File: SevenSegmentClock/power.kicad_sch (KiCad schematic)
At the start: 0 parts

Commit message: Adding two more displays to show a degree and a percent symbols
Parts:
- added C?: 1uF, symbol Device:C_Polarized
- added C?: 470uF, symbol Device:C_Polarized
- added C?: 100nF, symbol Device:C
- added U?: LM2596S-3.3, Package_TO_SOT_SMD:TO-263-5_TabPin3, symbol Regulator_Switching:LM2596S-3.3
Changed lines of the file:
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@@
 (kicad_sch (version 20211123) (generator eeschema)
   (paper "A4")
+  (symbol (lib_id "Device:C_Polarized") (at 144.78 106.807 0) (unit 1)
+    (in_bom yes) (on_board yes) (fields_autoplaced)
+    (property "Reference" "C?" (id 0) (at 147.701 105.0833 0)
+      (effects (font (size 1.27 1.27)) (justify left))
+    )
+    (property "Value" "1uF" (id 1) (at 147.701 107.6202 0)
+      (effects (font (size 1.27 1.27)) (justify left))
+    )
+    (property "Footprint" "" (id 2) (at 145.7452 110.617 0)
+      (effects (font (size 1.27 1.27)) hide)
+    )
+    (property "Datasheet" "~" (id 3) (at 144.78 106.807 0)
+      (effects (font (size 1.27 1.27)) hide)
+    )
+    (pin "1")
+    (pin "2")
+  )
+  (symbol (lib_id "Regulator_Switching:LM2596S-3.3") (at 153.924 74.295 0) (unit 1)
+    (in_bom yes) (on_board yes) (fields_autoplaced)
+    (property "Reference" "U?" (id 0) (at 153.924 65.5152 0))
+    (property "Value" "LM2596S-3.3" (id 1) (at 153.924 68.0521 0))
+    (property "Footprint" "Package_TO_SOT_SMD:TO-263-5_TabPin3" (id 2) (at 155.194 80.645 0)
+      (effects (font (size 1.27 1.27) italic) (justify left) hide)
+    )
+    (property "Datasheet" "http://www.ti.com/lit/ds/symlink/lm2596.pdf" (id 3) (at 153.924 74.295 0)
+      (effects (font (size 1.27 1.27)) hide)
+    )
+    (pin "1")
+    (pin "2")
+    (pin "3")
+    (pin "4")
+    (pin "5")
+  )
+  (symbol (lib_id "Device:C_Polarized") (at 163.449 106.68 0) (unit 1)
+    (in_bom yes) (on_board yes) (fields_autoplaced)
+    (property "Reference" "C?" (id 0) (at 166.37 104.9563 0)
+      (effects (font (size 1.27 1.27)) (justify left))
+    )
+    (property "Value" "470uF" (id 1) (at 166.37 107.4932 0)
+      (effects (font (size 1.27 1.27)) (justify left))
+    )
+    (property "Footprint" "" (id 2) (at 164.4142 110.49 0)
+      (effects (font (size 1.27 1.27)) hide)
+    )
+    (property "Datasheet" "~" (id 3) (at 163.449 106.68 0)
+      (effects (font (size 1.27 1.27)) hide)
+    )
+    (pin "1")
+    (pin "2")
+  )
+  (symbol (lib_id "Device:C") (at 130.556 107.188 0) (unit 1)
+    (in_bom yes) (on_board yes) (fields_autoplaced)
+    (property "Reference" "C?" (id 0) (at 133.477 106.3533 0)
+      (effects (font (size 1.27 1.27)) (justify left))
+    )
+    (property "Value" "100nF" (id 1) (at 133.477 108.8902 0)
+      (effects (font (size 1.27 1.27)) (justify left))
+    )
+    (property "Footprint" "" (id 2) (at 131.5212 110.998 0)
+      (effects (font (size 1.27 1.27)) hide)
+    )
+    (property "Datasheet" "~" (id 3) (at 130.556 107.188 0)
+      (effects (font (size 1.27 1.27)) hide)
+    )
+    (pin "1")
+    (pin "2")
+  )
 )

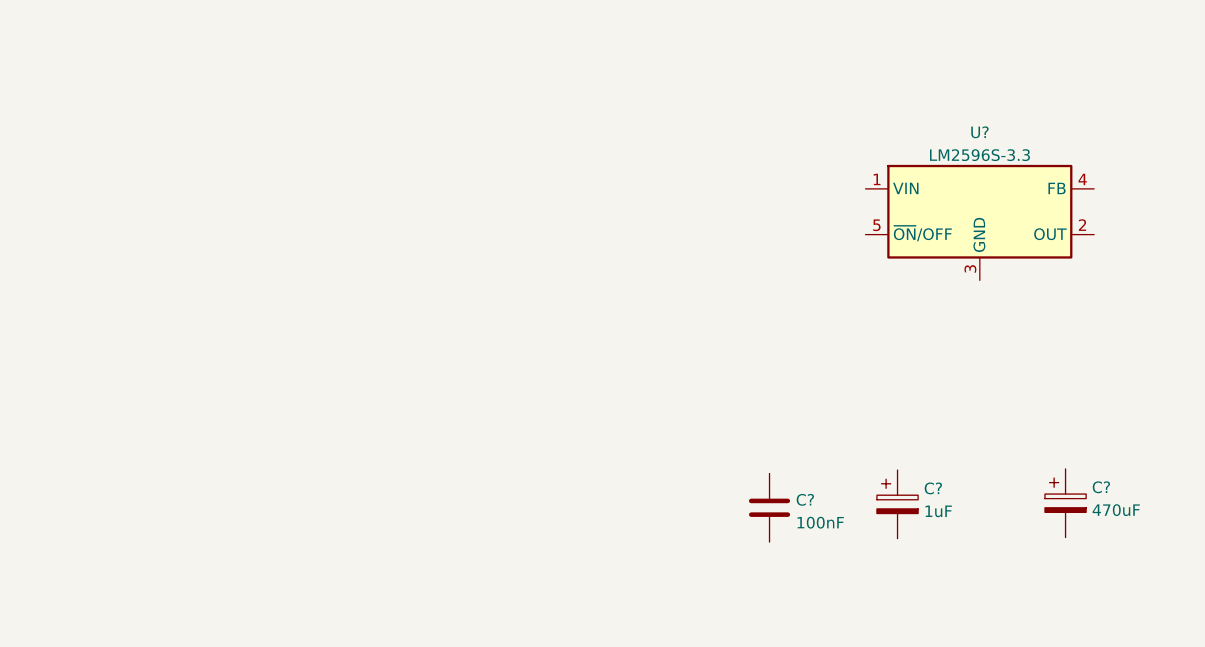
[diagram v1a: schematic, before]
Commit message: Adding the control schematic and fixing Eletrical Rules Checks
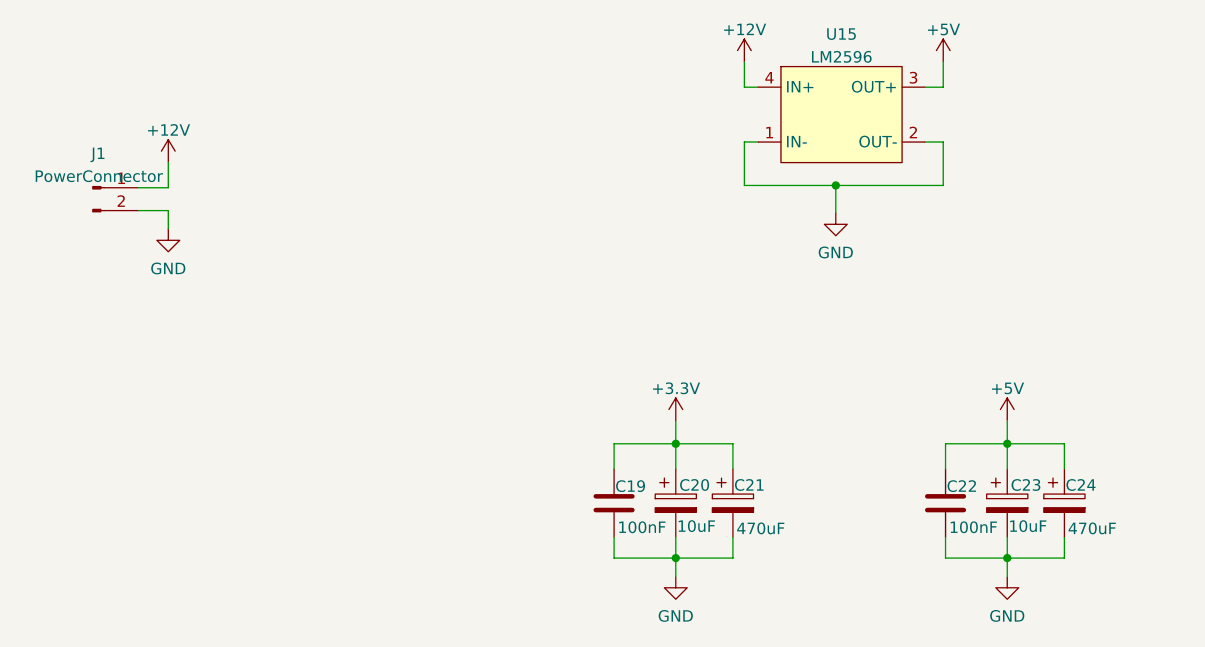
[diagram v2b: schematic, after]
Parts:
- removed U?: LM2596S-3.3, Package_TO_SOT_SMD:TO-263-5_TabPin3, symbol Regulator_Switching:LM2596S-3.3
- added C19: 100nF, symbol Device:C
- added C20: 10uF, symbol Device:C_Polarized
- added C21: 470uF, symbol Device:C_Polarized
- added J1: PowerConnector, symbol Library:PowerConnector
- added U15: LM2596, symbol Library:LM2596
- C23: renamed from C?; value 1uF -> 10uF
- gave numbers to parts that had none: 2
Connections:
- net +5V: now reaches C23.1
- net +5V: now also C22.1, C24.1, U15.3 (OUT+)
- net GND: now reaches C23.2
- net GND: now also C22.2, C24.2, C19.2, C20.2, C21.2, J1.2 (GND), U15.1 (IN-), U15.2 (OUT-)
- new net +12V: J1.1 (Pin_1), U15.4 (IN+)
- new net +3.3V: C19.1, C20.1, C21.1
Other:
- moved on the sheet: C22, C23

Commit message: Assigning footprints
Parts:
- removed J1: PowerConnector, symbol Library:PowerConnector
- added C26, C27: 470uF, Capacitor_THT:CP_Radial_D10.0mm_P5.00mm, symbol Device:C_Polarized
- added J1: 12V, Connector_PinHeader_2.54mm:PinHeader_1x01_P2.54mm_Vertical, symbol Library:PowerConnector_01
- added J2: GND, Connector_PinHeader_2.54mm:PinHeader_1x01_P2.54mm_Vertical, symbol Library:PowerConnector_01
- C19, C22: footprint (none) -> Capacitor_THT:C_Disc_D6.0mm_W2.5mm_P5.00mm
- C20: value 10uF -> 47uF; footprint (none) -> Capacitor_THT:CP_Radial_D6.3mm_P2.50mm
- C21: value 470uF -> 4.7uF; footprint (none) -> Capacitor_THT:CP_Radial_D6.3mm_P2.50mm
- C23: value 10uF -> 4.7uF; footprint (none) -> Capacitor_THT:CP_Radial_D6.3mm_P2.50mm
- C24: value 470uF -> 47uF; footprint (none) -> Capacitor_THT:CP_Radial_D6.3mm_P2.50mm
- U15: footprint (none) -> Library:LM2596
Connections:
- net +3.3V is gone; now on net +12V: C19.1, C20.1, C21.1
- net +12V: now also C26.1, J1.1 (Pin_1)
- net +5V: now also C27.1
- net GND: now also C26.2, C27.2, J2.1 (Pin_1)

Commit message: WIP: PCB design
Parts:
- C19, C22: footprint Capacitor_THT:C_Disc_D6.0mm_W2.5mm_P5.00mm -> Capacitor_SMD:C_1206_3216Metric_Pad1.33x1.80mm_HandSolder
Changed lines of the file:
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@@
       (effects (font (size 1.27 1.27)) (justify left))
     )
-    (property "Footprint" "Capacitor_THT:C_Disc_D6.0mm_W2.5mm_P5.00mm" (id 2) (at 114.2492 110.49 0)
+    (property "Footprint" "Capacitor_SMD:C_1206_3216Metric_Pad1.33x1.80mm_HandSolder" (id 2) (at 114.2492 110.49 0)
       (effects (font (size 1.27 1.27)) hide)
     )
@@
       (effects (font (size 1.27 1.27)) (justify left))
     )
-    (property "Footprint" "Capacitor_THT:C_Disc_D6.0mm_W2.5mm_P5.00mm" (id 2) (at 151.0792 110.49 0)
+    (property "Footprint" "Capacitor_SMD:C_1206_3216Metric_Pad1.33x1.80mm_HandSolder" (id 2) (at 151.0792 110.49 0)
       (effects (font (size 1.27 1.27)) hide)
     )
